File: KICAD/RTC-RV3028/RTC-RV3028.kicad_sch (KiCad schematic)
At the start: 8 parts, among them J4 Conn_01x05_Male, Y1 RV-3028-C7_32.768kHz_1ppm_TA_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

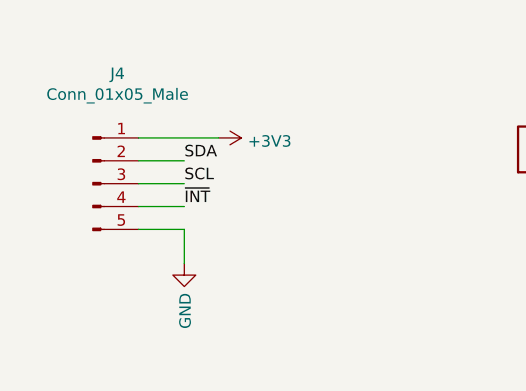
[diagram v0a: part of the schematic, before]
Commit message: corrected hibernate
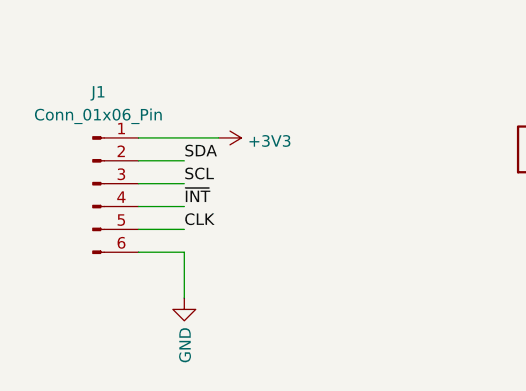
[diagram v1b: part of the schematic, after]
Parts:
- removed J4: Conn_01x05_Male, Connector_PinHeader_2.54mm:PinHeader_1x05_P2.54mm_Vertical, symbol Connector:Conn_01x05_Pin
- added J1: Conn_01x06_Pin, Connector_PinHeader_2.54mm:PinHeader_1x06_P2.54mm_Vertical, symbol Connector:Conn_01x06_Pin
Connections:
- net +3V3: now also J1.1 (Pin_1)
- net CLK: now also J1.5 (Pin_5)
- net GND: now also J1.6 (Pin_6)
- net SCL: now also J1.3 (Pin_3)
- net SDA: now also J1.2 (Pin_2)
- net ~{INT}: now also J1.4 (Pin_4)
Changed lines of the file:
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@@
-	(wire
-		(pts
-			(xy 88.9 81.28) (xy 88.9 77.47)
-		)
-		(stroke
-			(width 0)
-			(type default)
-		)
-	)
 	(wire
 		(pts
@@
 	(wire
 		(pts
+			(xy 83.82 77.47) (xy 88.9 77.47)
+		)
+		(stroke
+			(width 0)
+			(type default)
+		)
+	)
+	(wire
+		(pts
+			(xy 88.9 80.01) (xy 88.9 85.09)
+		)
+		(stroke
+			(width 0)
+			(type default)
+		)
+	)
+	(wire
+		(pts
 			(xy 146.05 71.12) (xy 132.08 71.12)
 		)
@@
 	(wire
 		(pts
+			(xy 83.82 80.01) (xy 88.9 80.01)
+		)
+		(stroke
+			(width 0)
+			(type default)
+		)
+	)
+	(wire
+		(pts
 			(xy 185.42 62.23) (xy 185.42 60.96)
 		)
@@
 		(pts
 			(xy 185.42 59.69) (xy 185.42 60.96)
-		)
-		(stroke
-			(width 0)
-			(type default)
-		)
-	)
-	(wire
-		(pts
-			(xy 83.82 77.47) (xy 88.9 77.47)
 		)
 		(stroke
@@
 	(label "SCL"
 		(at 132.08 76.2 0)
+		(effects
+			(font
+				(size 1.27 1.27)
+			)
+			(justify left bottom)
+		)
+	)
+	(label "CLK"
+		(at 88.9 77.47 0)
 		(effects
 			(font
@@
 	(symbol
 		(lib_id "power:GND")
-		(at 88.9 81.28 0)
+		(at 88.9 85.09 0)
 		(unit 1)
 		(body_style 1)
@@
 		(dnp no)
 		(property "Reference" "#PWR0108"
-			(at 88.9 87.63 0)
+			(at 88.9 91.44 0)
 			(hide yes)
 			(show_name no)
@@
 		)
 		(property "Value" "GND"
-			(at 89.027 84.5312 90)
+			(at 89.027 88.3412 90)
 			(show_name no)
 			(do_not_autoplace no)
@@
 		)
 		(property "Footprint" ""
-			(at 88.9 81.28 0)
+			(at 88.9 85.09 0)
 			(hide yes)
 			(show_name no)
@@
 		)
 		(property "Datasheet" ""
-			(at 88.9 81.28 0)
+			(at 88.9 85.09 0)
 			(hide yes)
 			(show_name no)
@@
 		)
 		(property "Description" ""
-			(at 88.9 81.28 0)
+			(at 88.9 85.09 0)
 			(show_name no)
 			(do_not_autoplace no)
@@
 			)
 		)
-		(property "Description" "FC0H104ZFTBR24"
+		(property "Description" "FC0H224ZFTBR24"
 			(at 200.66 81.28 0)
 			(hide yes)
@@
 	)
 	(symbol
-		(lib_id "Connector:Conn_01x05_Pin")
+		(lib_id "Connector:Conn_01x06_Pin")
 		(at 78.74 72.39 0)
 		(unit 1)
@@
 		(in_pos_files yes)
 		(dnp no)
-		(property "Reference" "J4"
-			(at 81.4832 60.1726 0)
-			(show_name no)
-			(do_not_autoplace no)
-			(effects
-				(font
-					(size 1.27 1.27)
-				)
-			)
-		)
-		(property "Value" "Conn_01x05_Male"
-			(at 81.4832 62.484 0)
-			(show_name no)
-			(do_not_autoplace no)
-			(effects
-				(font
-					(size 1.27 1.27)
-				)
-			)
-		)
-		(property "Footprint" "Connector_PinHeader_2.54mm:PinHeader_1x05_P2.54mm_Vertical"
+		(fields_autoplaced yes)
+		(property "Reference" "J1"
+			(at 79.375 62.23 0)
+			(show_name no)
+			(do_not_autoplace no)
+			(effects
+				(font
+					(size 1.27 1.27)
+				)
+			)
+		)
+		(property "Value" "Conn_01x06_Pin"
+			(at 79.375 64.77 0)
+			(show_name no)
+			(do_not_autoplace no)
+			(effects
+				(font
+					(size 1.27 1.27)
+				)
+			)
+		)
+		(property "Footprint" "Connector_PinHeader_2.54mm:PinHeader_1x06_P2.54mm_Vertical"
 			(at 78.74 72.39 0)
 			(hide yes)
@@
 			)
 		)
-		(property "Description" "Generic connector, single row, 01x05, script generated"
+		(property "Description" "Generic connector, single row, 01x06, script generated"
 			(at 78.74 72.39 0)
 			(hide yes)
@@
 			)
 		)
+		(pin "3"
+		)
+		(pin "4"
+		)
+		(pin "5"
+		)
+		(pin "2"
+		)
 		(pin "1"
 		)
-		(pin "2"
-		)
-		(pin "3"
-		)
-		(pin "4"
-		)
-		(pin "5"
+		(pin "6"
 		)
 		(instances
 			(project "RTC-RV3028"
 				(path "/b9be8b78-2ac5-4dd5-abc0-89a2c2dea7e6"
-					(reference "J4")
+					(reference "J1")
 					(unit 1)
 				)
